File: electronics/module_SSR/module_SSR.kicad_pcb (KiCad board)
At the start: 2 copper layers, 2 parts

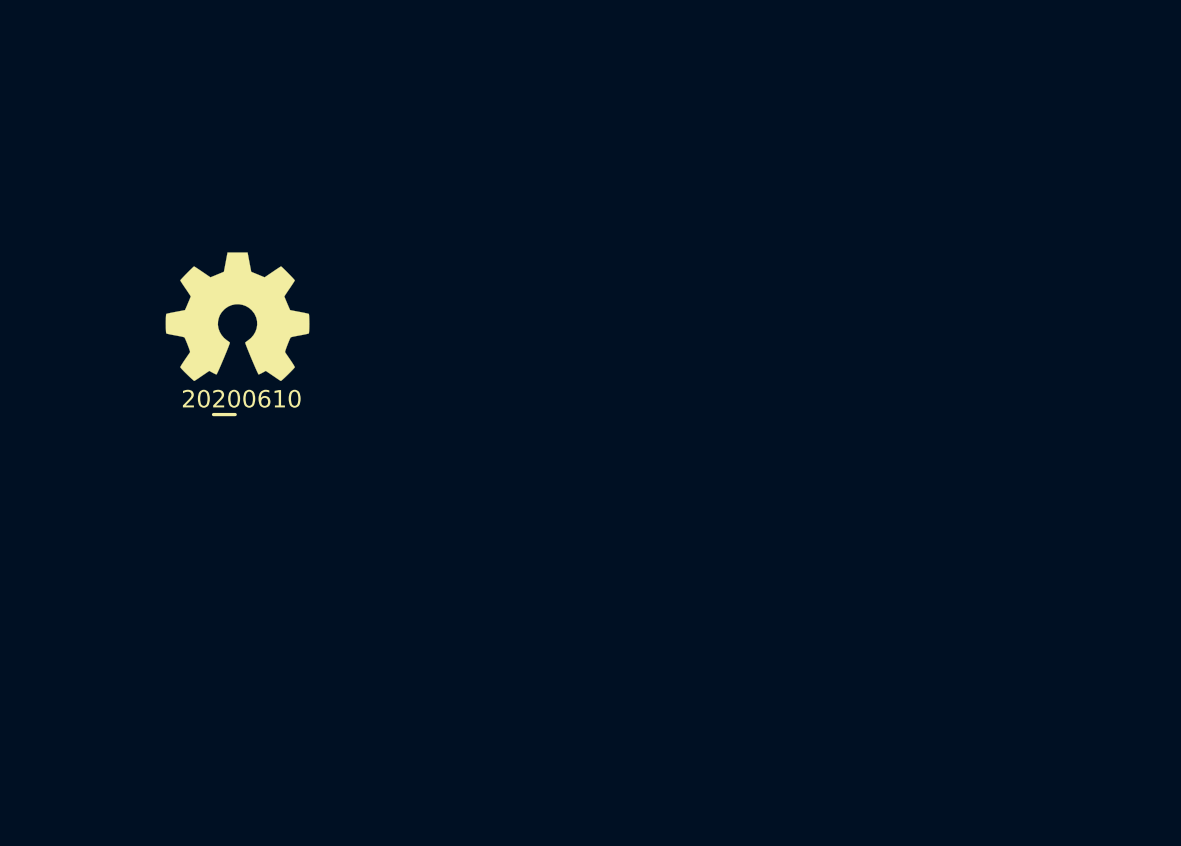
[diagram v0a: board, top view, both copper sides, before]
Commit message: added mounting holes, initial PCB sizing
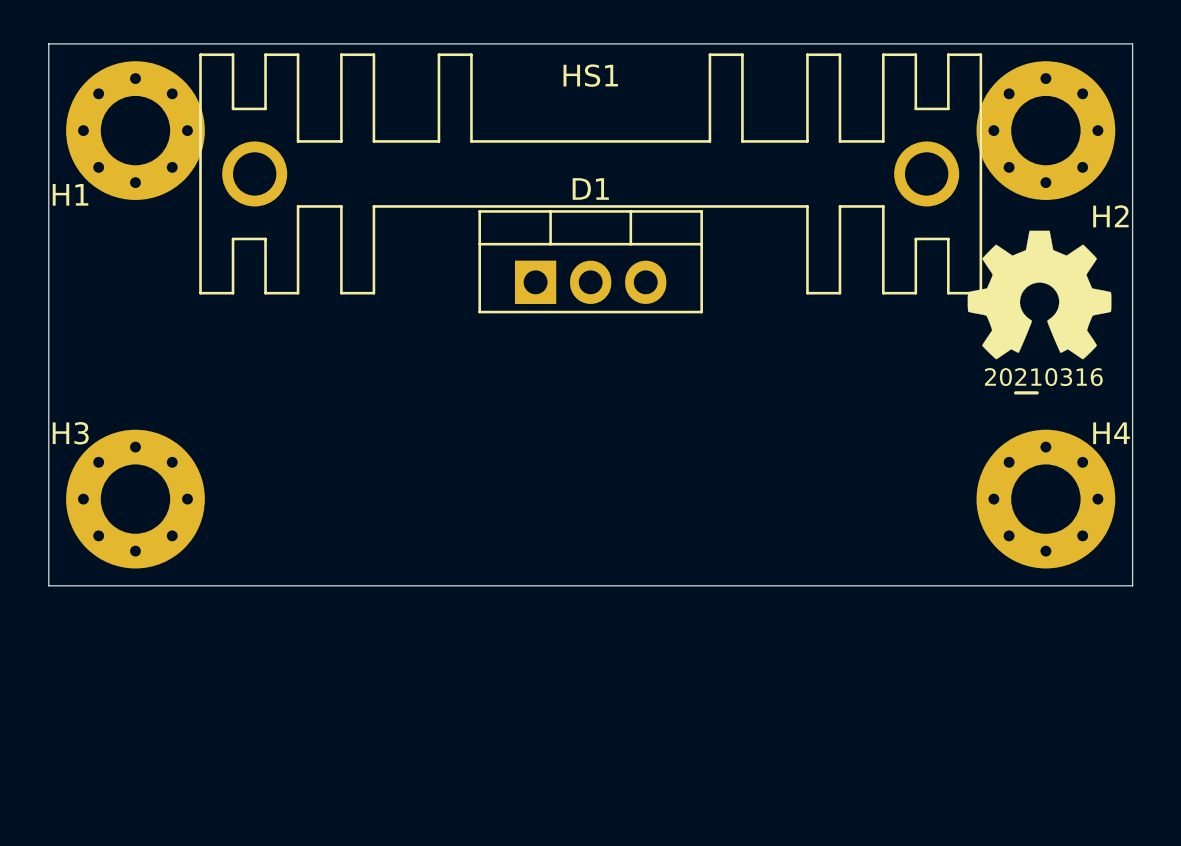
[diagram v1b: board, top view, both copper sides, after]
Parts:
- added D1: Q_TRIAC_A1A2G, Package_TO_SOT_THT:TO-220-3_Vertical, F.Cu at (152.5, 86.0)
- added H1: M3, MountingHole:MountingHole_3.2mm_M3_Pad_Via, F.Cu at (134.0, 79.0)
- added H2: M3, MountingHole:MountingHole_3.2mm_M3_Pad_Via, F.Cu at (176.0, 79.0)
- added H3: M3, MountingHole:MountingHole_3.2mm_M3_Pad_Via, F.Cu at (134.0, 96.0)
- added H4: M3, MountingHole:MountingHole_3.2mm_M3_Pad_Via, F.Cu at (176.0, 96.0)
- added HS1: XSD683-022, SquantorHeatsink:XSD683-022, F.Cu at (155.0, 81.0)
- N1: value 20200610 -> 20210316
- moved N1 37.0 mm to (175.1, 90.5)
- moved N2 37.0 mm to (175.7, 86.6)
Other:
- board outline added: 50 x 25 mm

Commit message: schematic completed, placed and routed
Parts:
- added C1: 10n, Capacitor_THT:C_Disc_D14.5mm_W5.0mm_P7.50mm, F.Cu at (150.0, 105.0)
- added C2: 47n, Capacitor_THT:C_Disc_D14.5mm_W5.0mm_P7.50mm, F.Cu at (160.0, 105.0)
- added J1: Conn_01x02, SquantorPhoenixContact:MKDS_2conn_508pitch_1711725, F.Cu at (136.0, 93.0)
- added J2: Conn_01x02, Connector_Molex:Molex_KK-254_AE-6410-02A_1x02_P2.54mm_Vertical, F.Cu at (176.0, 100.0)
- added R1: 47, Resistor_THT:R_Axial_DIN0309_L9.0mm_D3.2mm_P12.70mm_Horizontal, F.Cu at (145.0, 92.3)
- added R2: 330, Resistor_THT:R_Axial_DIN0309_L9.0mm_D3.2mm_P12.70mm_Horizontal, F.Cu at (165.0, 92.3)
- added R3: 470, Resistor_THT:R_Axial_DIN0309_L9.0mm_D3.2mm_P12.70mm_Horizontal, F.Cu at (155.0, 92.3)
- added R4: 1K, SquantorRcl:R_0603_hand, F.Cu at (178.0, 92.0)
- added U1: MOC3021M, Package_DIP:DIP-6_W7.62mm, F.Cu at (176.0, 94.0)
- D1: footprint Package_TO_SOT_THT:TO-220-3_Vertical -> SquantorIC:TO-220-3_Vertical_stagger
- N1, N2: moved to B.Cu
- moved N2 21.5 mm to (155.2, 80.2), turned to 180 degrees
- moved N1 20.3 mm to (155.8, 84.1), turned to 180 degrees
- moved H3 10.0 mm to (134.0, 106.0)
- moved H4 10.0 mm to (176.0, 106.0)
- moved D1 2.57 mm to (155.0, 85.6)
- moved HS1 0.40 mm to (155.0, 80.6)
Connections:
- D1 pad 1: Net-(D1-Pad1) -> /SWITCH
- D1 pad 2: Net-(D1-Pad2) -> /LIVE
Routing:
- net Earth: track 0.00 -> 103.3 mm
- net /SWITCH: track 0.00 -> 36.5 mm
- net /LIVE: track 0.00 -> 22.7 mm
- net Net-(D1-Pad3): track 0.00 -> 11.7 mm
- net Net-(C2-Pad1): track 0.00 -> 10.0 mm
- net /LED_A: track 0.00 -> 9.49 mm
- net /LED_C: track 0.00 -> 6.34 mm
- net Net-(C1-Pad1): track 0.00 -> 5.00 mm
- net Net-(R2-Pad1): track 0.00 -> 4.49 mm
- net Net-(R4-Pad1): track 0.00 -> 2.13 mm
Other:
- board size 50 x 25 mm -> 50 x 35 mm

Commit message: updated versionnumber, some silk changes
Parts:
- N1: value 20210316 -> 20210317
- moved R4 0.30 mm to (178.0, 92.3)

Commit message: reviewed SSR module
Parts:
- D1: value Q_TRIAC_A1A2G -> BTA16-600CRG
- N1: value 20210317 -> 20210321
